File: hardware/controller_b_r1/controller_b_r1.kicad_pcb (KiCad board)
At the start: 2 copper layers, 130.1 x 23.8 mm, 59 parts, among them J101 Front Pannel Conn, J102 2x5 Mini SWD Header, J103 USB Micro B, Q101 Q_Dual_NMOS_S1G1D2S2G2D1, SW101 BUTTON_2, SW102 BUTTON_1, U101 NCP115ASN330T2G, U102 74LVC2T45HK3, U103 RP2040, U104 W25Q16JVUXIQ, Y101 12MHz

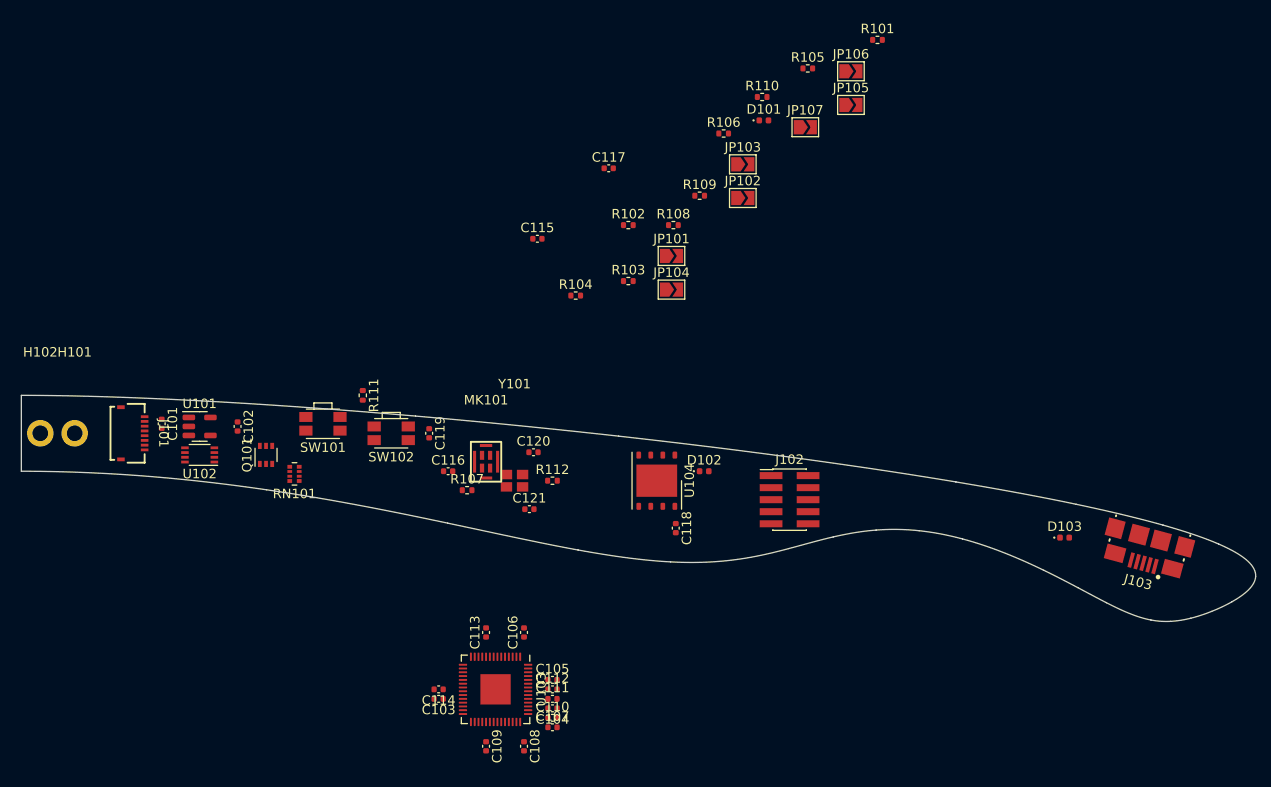
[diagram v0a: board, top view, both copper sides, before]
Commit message: Refined schematic and layout:
- Removed some caps from the user buttons, mcu reset and power reg enable because datasheets/example designs didn't have them (hopefully I don't regret it).
- Removed pullups from the user buttons because I can use the RP2040 GPIO internal pullups.
- Changed a few res values to simplify the BOM.
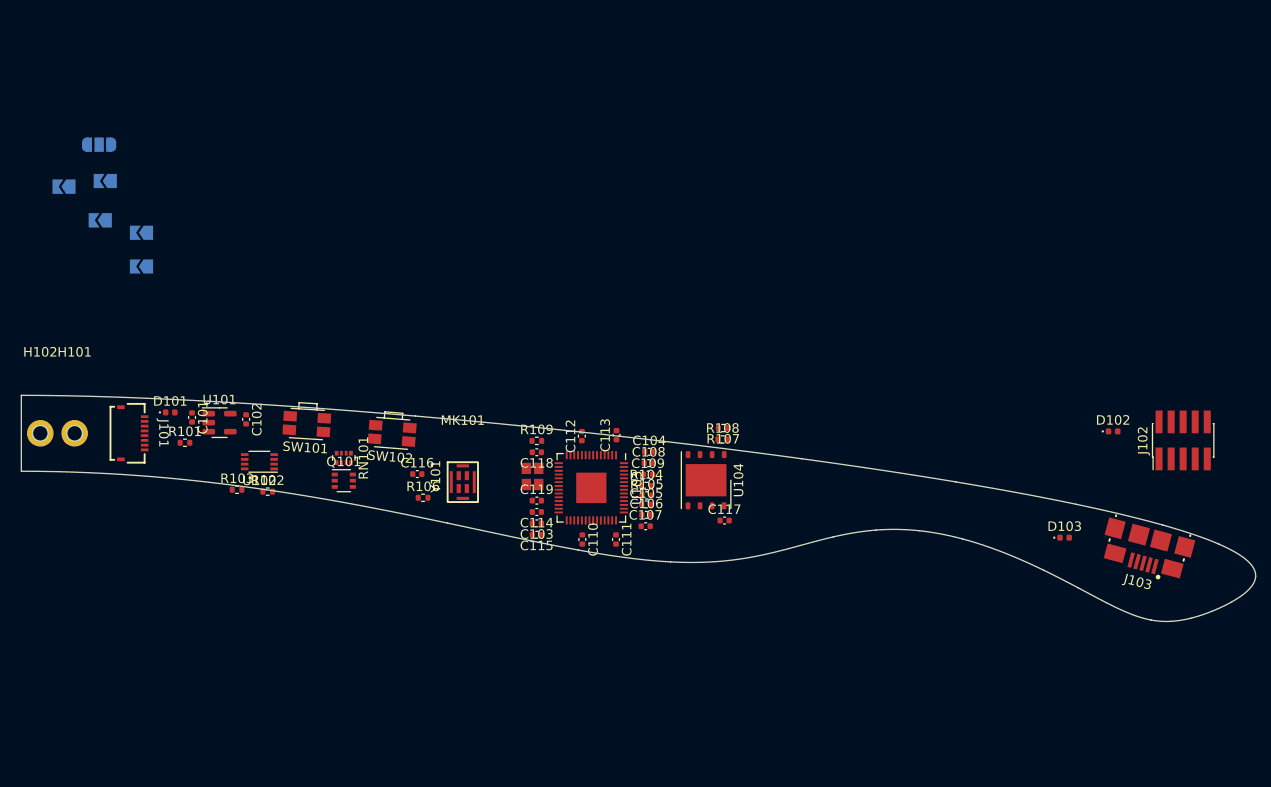
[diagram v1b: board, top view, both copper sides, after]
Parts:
- removed the C117 at (161.9, 72.1)
- removed C120, C121: 10p, Capacitor_SMD:C_0402_1005Metric
- removed JP107: SolderJumper_2_Open, Jumper:SolderJumper-2_P1.3mm_Open_TrianglePad1.0x1.5mm
- removed R110: 100R, Resistor_SMD:R_0402_1005Metric
- removed R111: 100k, Resistor_SMD:R_0402_1005Metric
- removed R112: 1k, Resistor_SMD:R_0402_1005Metric
- added C118: 10p, Capacitor_SMD:C_0402_1005Metric, F.Cu at (154.3, 102.0)
- C119: value 100n -> 10p
- J101: value Front Pannel Conn -> Front Pannel Connector
- J102: value 2x5 Mini SWD Header -> SWD Header
- JP101, JP102, JP103, JP105, JP106: moved to B.Cu
- JP104: value SolderJumper_2_Open -> SolderJumper_3_Open; footprint Jumper:SolderJumper-2_P1.3mm_Open_TrianglePad1.0x1.5mm -> Jumper:SolderJumper-3_P1.3mm_Open_RoundedPad1.0x1.5mm; moved to B.Cu
- Q101: value Q_Dual_NMOS_S1G1D2S2G2D1 -> NMOS
- R102: value DNP -> 10k
- R103: value 33k -> DNP
- R104: value 100R -> 27R
- R106: value 27R -> 10k
- R107: value 100k -> 10k
- R108, R109: value 10k -> 1k
- RN101: value R_Pack04_Split -> 10k
- SW101: value BUTTON_2 -> Reset Button
- SW102: value BUTTON_1 -> User Button
- moved R101 84.5 mm to (117.2, 101.0)
- moved JP106 83.9 mm to (104.5, 74.0), turned to 180 degrees
- moved JP105 80.1 mm to (108.3, 77.5), turned to 180 degrees
- moved D101 69.8 mm to (115.7, 97.8)
- moved JP103 67.2 mm to (108.8, 73.4), turned to 180 degrees
- moved JP102 63.8 mm to (112.7, 82.4), turned to 180 degrees
- moved JP104 62.3 mm to (108.2, 69.6), turned to 180 degrees
- moved JP101 55.9 mm to (112.7, 78.9), turned to 180 degrees
- moved R106 49.8 mm to (142.4, 106.8)
- moved R105 48.1 mm to (165.9, 106.5)
- moved R102 47.3 mm to (126.0, 106.2)
- moved R103 46.8 mm to (122.7, 106.0)
- moved D102 43.3 mm to (215.1, 99.8)
- moved J102 42.0 mm to (222.5, 100.8), turned to 90 degrees
- moved C109 33.4 mm to (166.1, 104.3), turned to 0 degrees
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- renumbered C118 to C117
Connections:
- C115 pad 1: /3V3_EN -> /nRESET
- C119 pad 1: /USER_BUTTON_1 -> GND
- C119 pad 2: GND -> /OSC_IN
- JP101 pad 1: Net-(JP101-Pad1) -> /nRESET_SWD
- JP101 pad 2: /USER_BUTTON_2 -> /nRESET
- JP103 pad 1: +5V -> VBUS
- JP103 pad 2: VBUS -> +5V
- JP104 pad 2: Net-(JP101-Pad1) -> /RESET_BUTTON
- JP105 pad 1: Net-(JP101-Pad1) -> /RESET_BUTTON
- JP105 pad 2: /nRESET -> /USER_BUTTON_2
- JP106 pad 1: /nRESET_SWD -> GND
- JP106 pad 2: /nRESET -> /BOOTSEL
- MK101 pad 3: Net-(MK101-Pad3) -> /MIC_SELECT
- R101 pad 1: /LED_SPI_DIR -> /3V3_EN
- R101 pad 2: +3V3 -> +5V
- R102 pad 1: GND -> /LED_SPI_DIR
- R102 pad 2: /LED_SPI_DIR -> +3V3
- R103 pad 1: /3V3_EN -> GND
- R103 pad 2: +5V -> /LED_SPI_DIR
- R104 pad 1: Net-(JP101-Pad1) -> /USB_D_P
- R104 pad 2: /nRESET_SW -> /USB_D_TERM_P
- R105 pad 1: /USB_D_P -> /USB_D_N
- R105 pad 2: /USB_D_TERM_P -> /USB_D_TERM_N
- R106 pad 1: /USB_D_N -> +3V3
- R106 pad 2: /USB_D_TERM_N -> /MIC_SELECT
- R107 pad 1: +3V3 -> /FLASH_nCS
- R107 pad 2: Net-(MK101-Pad3) -> +3V3
- R108 pad 1: /nRESET -> /BOOTSEL
- R108 pad 2: +3V3 -> /FLASH_nCS
- R109 pad 1: /FLASH_nCS -> /OSC_OUT_DIV
- R109 pad 2: +3V3 -> /OSC_OUT
- SW101 pad 2: /nRESET_SW -> /RESET_BUTTON
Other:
- outline, holes or cut-outs redrawn

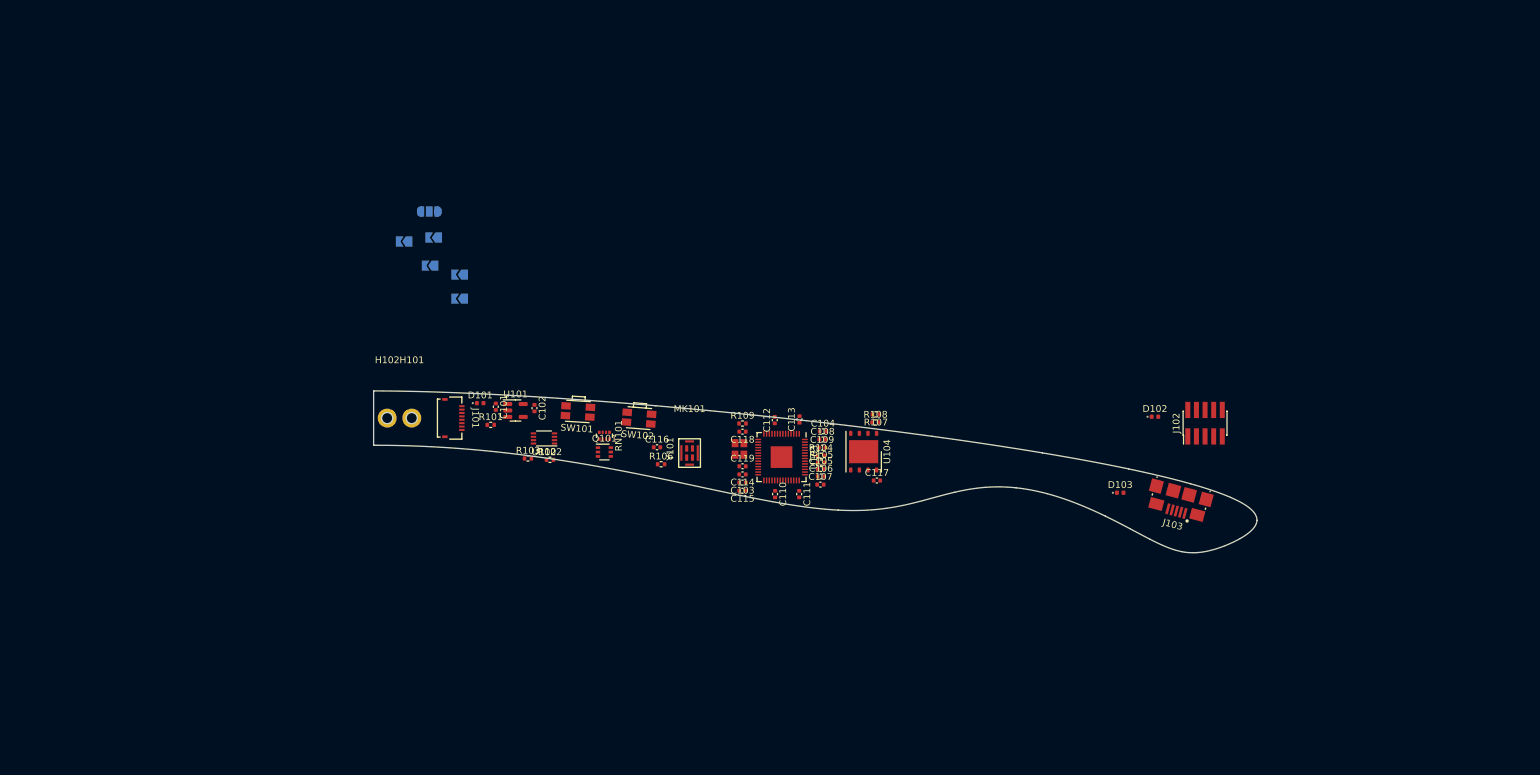
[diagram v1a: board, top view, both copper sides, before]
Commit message: Controller board is pretty much done. USB impedance will need to be tweaked and DRC checks done once a PCB fab is decided on. Having all the serial interfaces routed from the same side (the top) of the MCU was a pain, will have to keep an eye out for EMI problems. Also restricting the board to 2 layers was probably not worth all the extra routing effort.
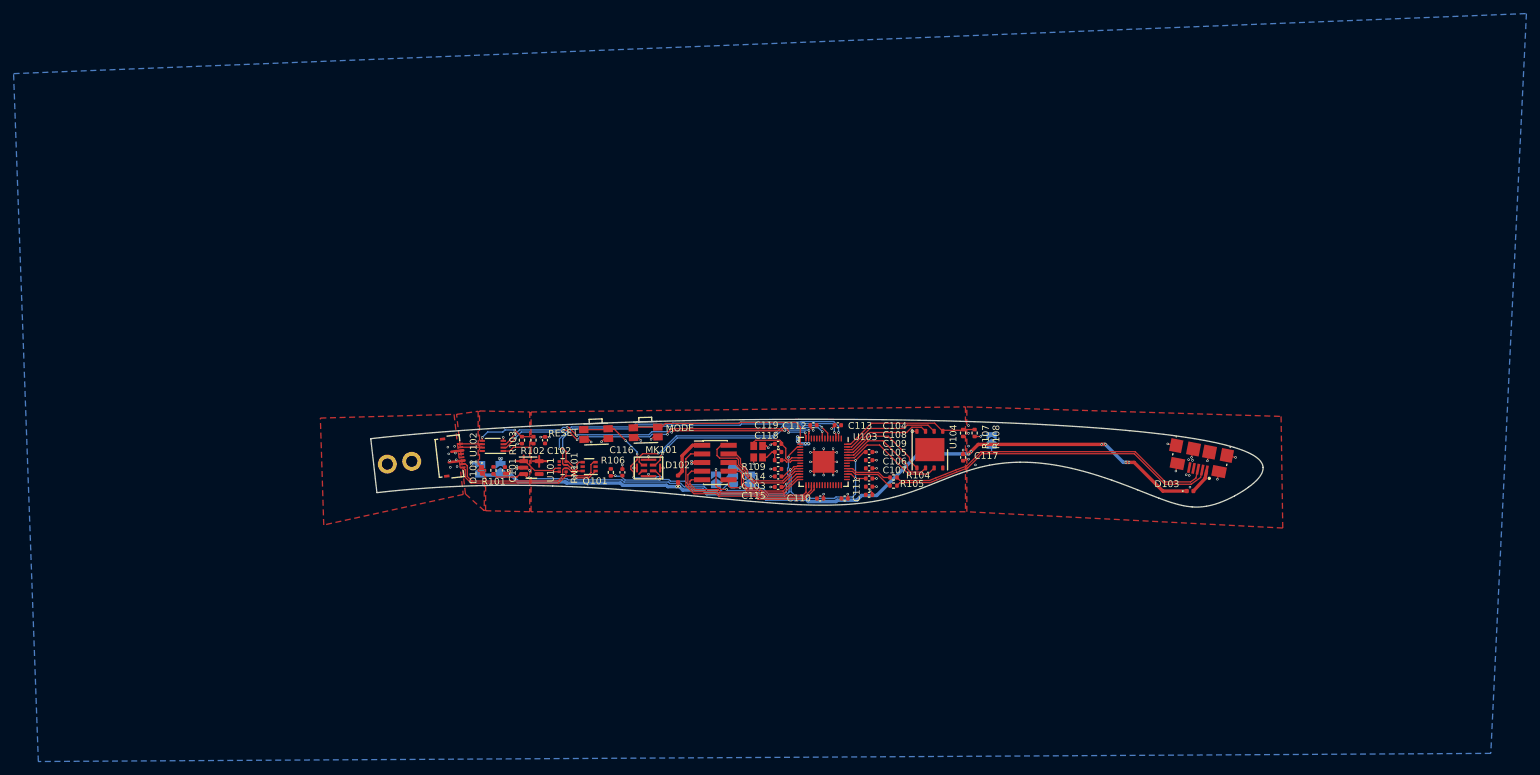
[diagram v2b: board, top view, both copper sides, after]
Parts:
- moved JP106 91.4 mm to (191.1, 103.3), turned to 90 degrees
- moved J102 72.4 mm to (150.3, 106.5), turned to 0 degrees
- moved D102 70.9 mm to (144.8, 109.0), turned to 90 degrees
- moved JP104 59.3 mm to (152.9, 108.5), turned to 90 degrees
- moved JP105 52.6 mm to (150.4, 109.1), turned to 90 degrees
- moved JP101 52.4 mm to (155.4, 109.1), turned to 90 degrees
- moved JP103 35.5 mm to (118.7, 107.5), turned to 90 degrees
- moved JP102 25.3 mm to (115.7, 107.5), turned to 90 degrees
- moved R108 14.7 mm to (188.6, 102.2), turned to 90 degrees
- moved C117 13.1 mm to (186.8, 105.8), turned to 90 degrees
- moved R107 13.1 mm to (186.8, 102.2), turned to -90 degrees
- moved R105 11.2 mm to (176.6, 110.0), turned to 180 degrees
- moved R104 11.2 mm to (176.6, 108.8), turned to 180 degrees
- moved D103 10.3 mm to (220.3, 110.8)
- moved D101 9.90 mm to (116.0, 107.7), turned to -90 degrees
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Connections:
- J101 pad 9: unconnected-(J101-Pad9) -> GND
- U102 pad 2: /LED_CLK_3V3 -> /LED_MOSI_3V3
- U102 pad 3: /LED_MOSI_3V3 -> /LED_CLK_3V3
- U102 pad 6: /LED_MOSI_5V0 -> /LED_CLK_5V0
- U102 pad 7: /LED_CLK_5V0 -> /LED_MOSI_5V0
- U103 pad 15: unconnected-(U103-Pad15) -> /USER_BUTTON_1
- U103 pad 16: unconnected-(U103-Pad16) -> /USER_BUTTON_2
- U103 pad 17: /USER_BUTTON_1 -> unconnected-(U103-Pad17)
- U103 pad 18: /USER_BUTTON_2 -> unconnected-(U103-Pad18)
- U103 pad 27: unconnected-(U103-Pad27) -> /DBG_LED_0
- U103 pad 28: unconnected-(U103-Pad28) -> /DBG_LED_1
- U103 pad 29: /DBG_LED_0 -> /DBG_LED_2
- U103 pad 34: /DBG_LED_1 -> unconnected-(U103-Pad34)
- U103 pad 36: /DBG_LED_2 -> unconnected-(U103-Pad36)
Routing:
- net VBUS: track 0.00 -> 114.3 mm, vias 0 -> 8
- net GND: track 0.00 -> 60.1 mm, vias 0 -> 75
- net /SPARE_0_3V3: track 0.00 -> 54.9 mm, vias 0 -> 4
- net /SPARE_1_3V3: track 0.00 -> 51.1 mm, vias 0 -> 2
- net /USB_D_N: track 0.00 -> 49.5 mm
- net /USB_D_P: track 0.00 -> 48.9 mm
- net /LED_MOSI_3V3: track 0.00 -> 48.5 mm, vias 0 -> 6
- net /LED_CLK_3V3: track 0.00 -> 48.3 mm, vias 0 -> 6
- net /3V3_EN: track 0.00 -> 37.0 mm, vias 0 -> 1
- net /MIC_MISO: track 0.00 -> 32.6 mm, vias 0 -> 2
- net /RESET_BUTTON: track 0.00 -> 29.5 mm, vias 0 -> 3
- net /MIC_CLK: track 0.00 -> 28.9 mm, vias 0 -> 2
- net +1V1: track 0.00 -> 28.2 mm, vias 0 -> 3
- net /USER_BUTTON_1: track 0.00 -> 27.8 mm
- net /DBG_UART_RX: track 0.00 -> 27.6 mm
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- added copper zone on F.Cu, net +3V3
- added copper zone on F.Cu, net +5V
- added copper zone on B.Cu, net GND
- added copper zone on F.Cu, net GND
- added copper zone on F.Cu, net VDD
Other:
- board size 130.1 x 23.8 mm -> 131.5 x 12.9 mm
- board text added: "MODE"
- board text added: "PASS THROUGH"
- board text added: "RESET"
- board text added: "RESET MCU"
- board text added: "RESET POWER"
- board text added: "SWD MCU RESET EN"
- board text added: "THIS BOARD ONLY"
- board text added: "USB BOOT EN"
- board text added: "USB/SWD PWR SEL"
- board text added: "USR BTN2 EN"

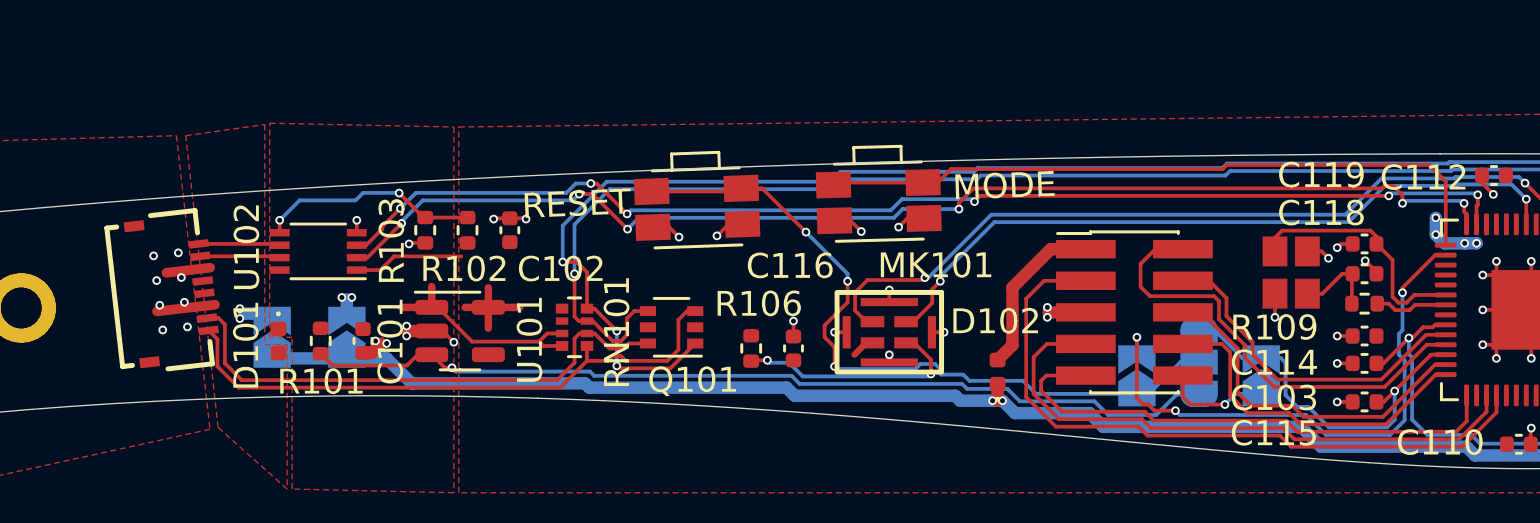
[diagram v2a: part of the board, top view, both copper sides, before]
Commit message: Display board layout is now 95% complete, the number of caps on the board might need some further tweaking and there are also some gaps where a few more LEDs could fit. Additionally I've decided to provide the option to use the hinges as the ground connection allowing more +5V channels on the FFC connectors which should mean more current carrying capacity. The new power board schematic has had some changes, namely the vreg has changed and so have some of the passives around it, more input protect has been added, a MOV for over voltage protection and an NMOS for reverse pol. Looking at the new vreg the power dissipation before it cooks itself (~1.1W) isn't great but it's enough for about 2.5A (at around 93% eff.) for the LEDs which hasn't usually been the bottleneck (looking at you 9V batteries). This means we're expecting around 1.8A peak input current at a Vin of 7V and need to size the fuze around that as much more current and the vreg is cooked. Might look into a over voltage shutout circuit if it seems like we're blowing fuses too often.
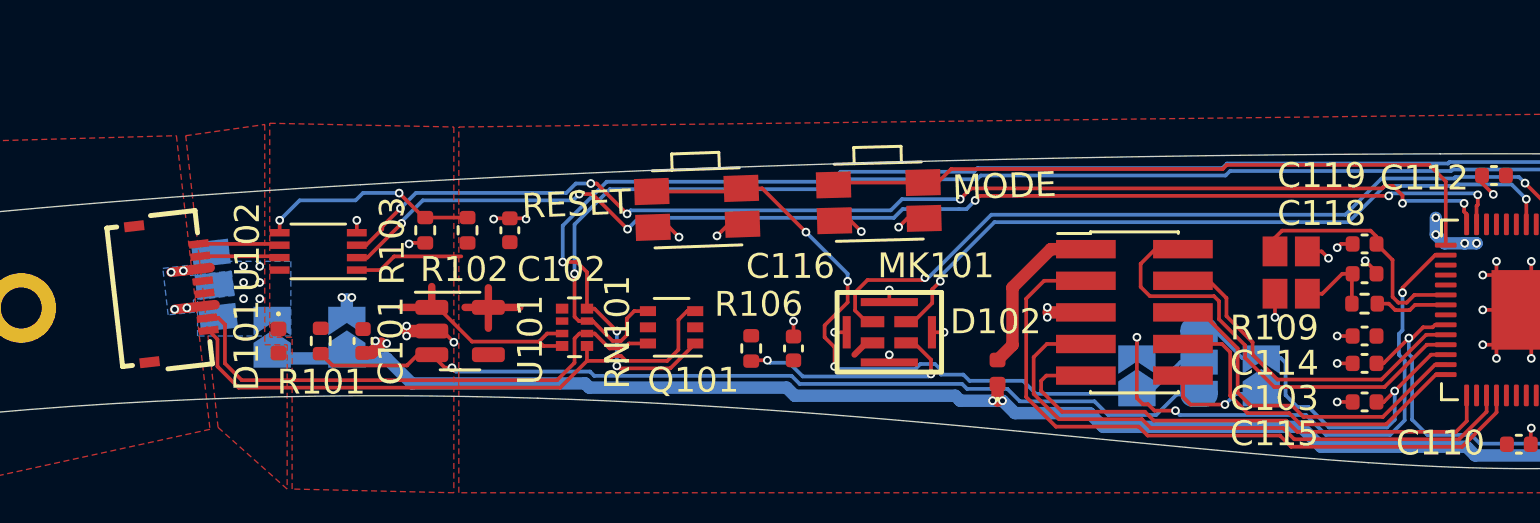
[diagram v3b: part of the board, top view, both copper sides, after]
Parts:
- added JP107: SolderJumper_3_Open, Jumper:SolderJumper-3_P1.3mm_Open_Pad1.0x1.5mm, B.Cu at (113.4, 105.5)
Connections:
- J101 pad 1: /LED_CLK_5V0 -> /LED_MOSI_5V0
- J101 pad 2: /LED_MOSI_5V0 -> /LED_CLK_5V0
- J101 pad 3: GND -> /VDD_OR_GND
- J101 pad 6: GND -> /VDD_OR_GND
- U102 pad 2: /LED_MOSI_3V3 -> /LED_CLK_3V3
- U102 pad 3: /LED_CLK_3V3 -> /LED_MOSI_3V3
- U102 pad 6: /LED_CLK_5V0 -> /LED_MOSI_5V0
- U102 pad 7: /LED_MOSI_5V0 -> /LED_CLK_5V0
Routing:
- net GND: track 60.1 -> 56.0 mm, vias 75 -> 67
- net /VDD_OR_GND: track 0.00 -> 3.21 mm, vias 0 -> 4
- net VDD: track 1.17 -> 0.00 mm, vias 2 -> 6
- added copper zone on B.Cu, net /VDD_OR_GND
- added copper zone on B.Cu, net VDD
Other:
- board text added: "PASS THR- OUGH"
- board text added: "PWR SEL"
- board text added: "VDD+GND CABLE SEL JUST VDD"
- board text removed: "PASS THROUGH"
- board text removed: "USB/SWD PWR SEL"
